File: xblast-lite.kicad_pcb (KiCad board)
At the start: 2 copper layers, 52 x 50.5 mm, 30 parts, among them J1 JTAG, J2 XBOX LPC, J3 GPIO, J4 LCD, J5 PLCC-32 Socket, Q1 BC846, Q2 BC846, U1 74LVC125, U3 XC9572XL-xxVQx44, U4 TPS27081A

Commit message: WIP increase trace widths
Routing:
- net /A15_CTRL: track 12.4 -> 10.9 mm
- net /XLCLK: track 45.3 -> 44.3 mm
- net /LCD_E: track 22.7 -> 21.9 mm, vias 0 -> 2
- net GND: vias 79 -> 77

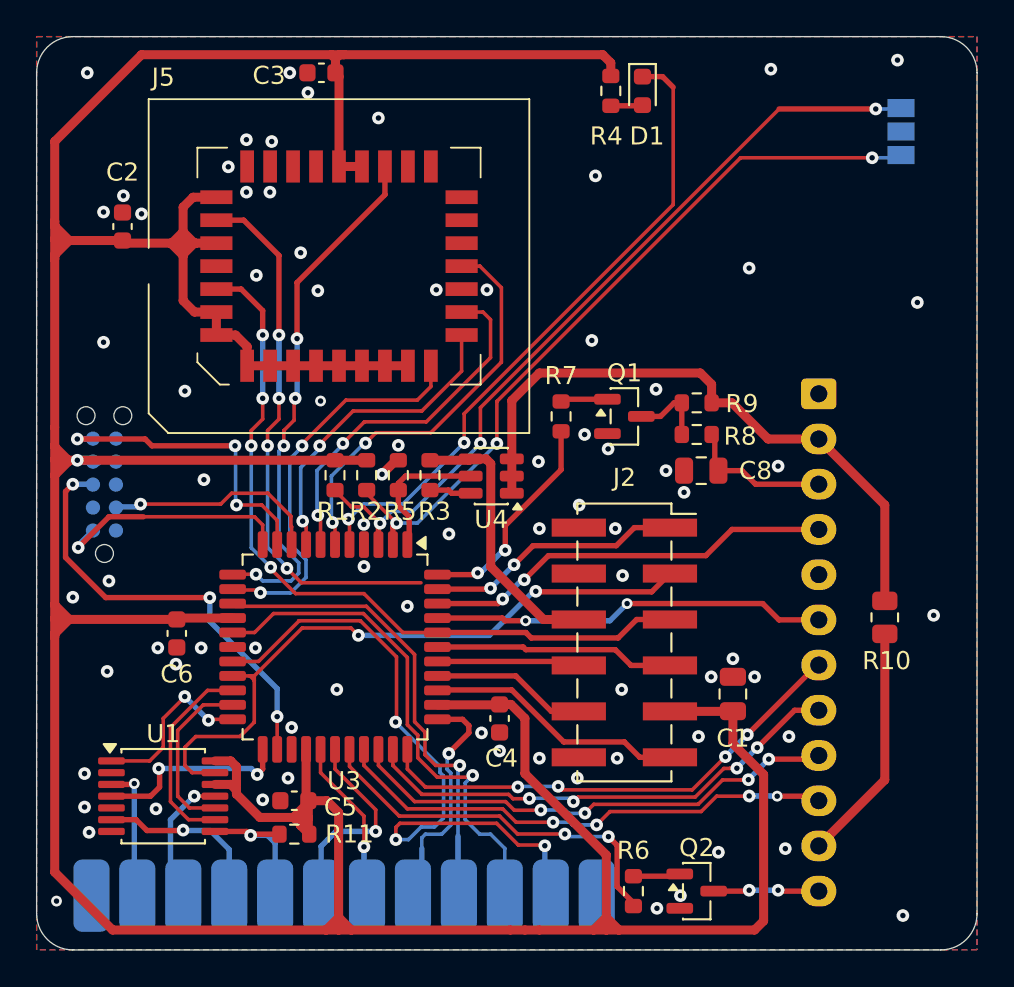
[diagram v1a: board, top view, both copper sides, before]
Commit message: Increase all track widths to 0.3mm min
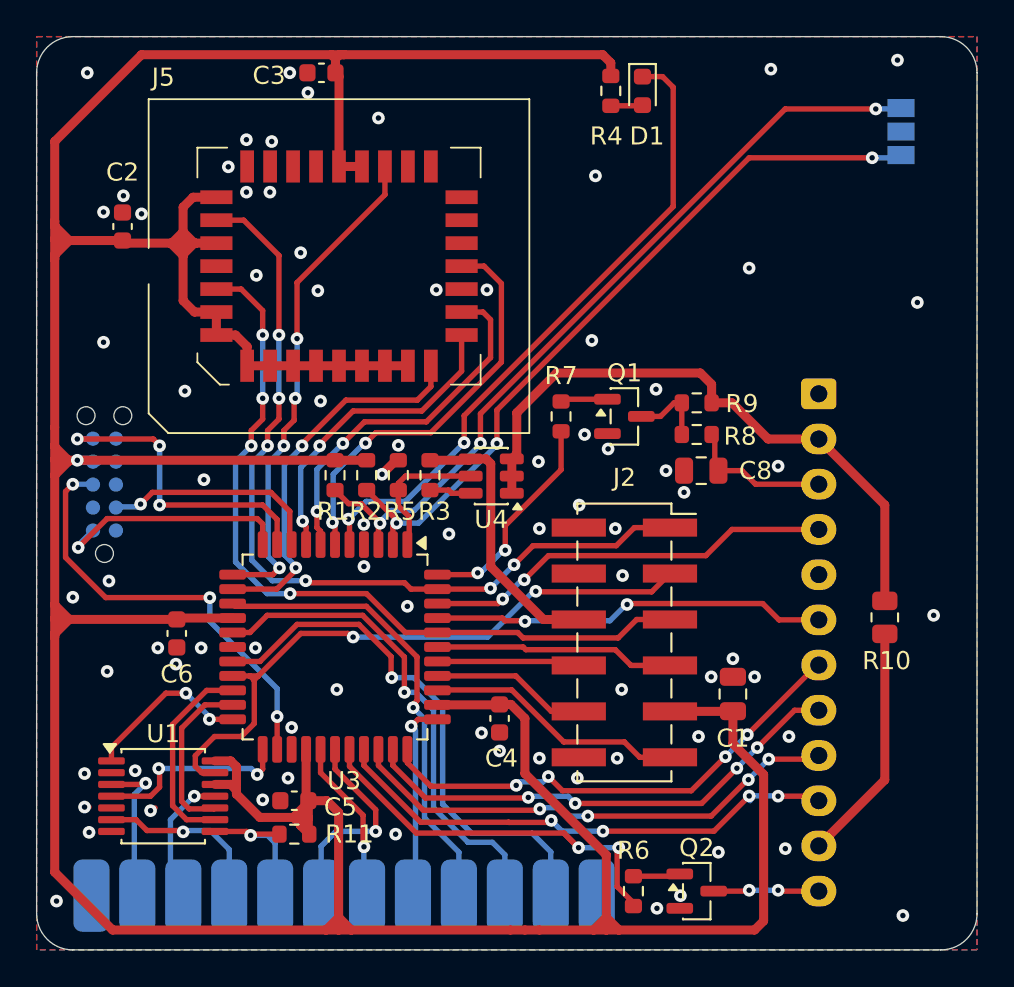
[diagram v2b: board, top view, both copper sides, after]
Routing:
- net /GPI0: track 36.4 -> 29.9 mm, vias 3 -> 1
- net /XLCLK: track 44.3 -> 46.9 mm
- net /~{XLRESET}: track 42.1 -> 43.8 mm
- net /~{FLFRAME}: track 29.4 -> 27.9 mm
- net /~{XLFRAME}: track 37.0 -> 35.5 mm
- net /GPO1: track 13.3 -> 11.8 mm
- net /LCD_BL: track 21.3 -> 22.4 mm
- net /GPI1: track 28.5 -> 27.5 mm
- net /FLAD0: track 22.1 -> 21.1 mm
- net /D0: track 7.55 -> 8.47 mm
- net /GPO0: track 26.5 -> 25.8 mm
- net +5V: track 35.3 -> 34.7 mm
- net GND: track 1.61 -> 1.85 mm, vias 77 -> 79

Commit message: Cleanup
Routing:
- net /FLAD3: track 22.8 -> 25.5 mm, vias 2 -> 0
- net /XLCLK: track 46.9 -> 49.5 mm, vias 6 -> 4
- net /FLAD2: track 20.3 -> 22.6 mm, vias 2 -> 0
- net /FLAD1: track 17.6 -> 19.5 mm, vias 2 -> 0
- net /FLAD0: track 21.1 -> 22.8 mm
- net /TMS: track 17.3 -> 15.8 mm
- net /~{FLFRAME}: track 27.9 -> 26.5 mm
- net GND: track 1.85 -> 0.56 mm, vias 79 -> 84
- net /LCD_BL: track 22.4 -> 21.1 mm, vias 2 -> 0
- net +3V3: track 258.1 -> 259.1 mm, vias 1 -> 13
- net /LCD_D7: track 28.8 -> 27.8 mm, vias 4 -> 0
- net /TCK: track 13.8 -> 13.1 mm
- net /LCD_D4: track 27.5 -> 26.8 mm, vias 4 -> 0
- net /TDO: track 24.5 -> 25.1 mm
- net /TDI: track 12.1 -> 11.6 mm
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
